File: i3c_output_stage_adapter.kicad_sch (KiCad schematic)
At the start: 52 parts, among them J1 PinSocket_2x12_P2.54mm_Drill1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, J2 PinSocket_2x6_P2.54mm_Drill1.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, J3 Molex_Nano-Fit_1x2_SMD_105430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, J4 PinHeader_2x5_P1.27mm_SMD, J5 PinHeader_2x5_P1.27mm_SMD, J6 JST_XH_1x3_S3B-XH-A-LF-SN, Q1 DMC2400UV-7, Q2 DMC2400UV-7, Q3 DMC2400UV-7, Q4 DMC2400UV-7, U1 TPS7A0518P_SOT23-5, U2 SN74LVC1G240_SC70, U3 SN74LVC1G240_SC70

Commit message: [#68164] Update schematic
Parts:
- removed D3: LED_G_0402_VLMTG1500-GS08, antmicro-footprints:LED_0402_1005Metric_G, symbol antmicroLEDIndicationDiscrete:LED_G_0402_VLMTG1500-GS08
- removed Q1, Q2: DMC2400UV-7, antmicro-footprints:SOT-563, symbol antmicroTransistorsFETsMOSFETsArrays:DMC2400UV-7
- removed R10, R19, R9: R_2k_0402, antmicro-footprints:R_0402_1005Metric, symbol antmicroResistors0402:R_2k_0402
- added MP1, MP2, MP3, MP4: MP_Pad6mm_Drill3.2mm, antmicro-footprints:MP_Pad6mm_Drill3.2mm, symbol antmicroMechanicalParts:MP_Pad6mm_Drill3.2mm
- added Q1, Q2: DMC31D5UDJ, antmicro-footprints:SOT-963, symbol antmicroTransistorsFETsMOSFETsArrays:DMC31D5UDJ
- added R10, R19, R20, R24: R_10k_0402, antmicro-footprints:R_0402_1005Metric, symbol antmicroResistors0402:R_10k_0402
- added R21, R25, R9: R_0R_0402, antmicro-footprints:R_0402_1005Metric, symbol antmicroResistors0402:R_0R_0402
- added R22, R23: R_2k_0402, antmicro-footprints:R_0402_1005Metric, symbol antmicroResistors0402:R_2k_0402
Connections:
- net +3V3: no longer R15.1
- net 1V8_LDO: no longer R17.2
- net GND: now also MP1.1, MP2.1, MP3.1, MP4.1, Q1.1 (S1), Q2.1 (S1), R10.1, R19.1, R23.1
- net SCL: now also J6.1, Q3.4 (S2), Q3.6 (D1), Q2.4 (S2), Q2.6 (D1); no longer J6.3
- net SCL_DOWN: now also R9.1; no longer Q3.2 (G1)
- net SCL_UP: now also R25.2; no longer Q3.5 (G2)
- net SDA: now also J6.3, Q1.4 (S2), Q1.6 (D1); no longer J6.1
- net SDA_DOWN: now also R15.1; no longer Q4.2 (G1)
- net SDA_UP: now also R21.2; no longer Q4.5 (G2)
- net at R6.1, R8.1: now also Q2.5 (G2)
- net at R2.2, R4.2: now also Q2.2 (G1)
- net at R1.2, R3.2: now also Q1.2 (G1)
- net at Q3.3 (D2): now also R22.1
- net at F1.1: now also Q1.3 (D2)
- net at R5.1, R7.1: now also Q1.5 (G2)
- net at F2.1: now also Q2.3 (D2)
- net at Q3.1 (S1): now also R23.2
- net VCC renamed +1V8
- net +1V8: now also R17.2, R20.2, R22.2, R24.2; no longer R15.2
- new net: Q4.5 (G2), R20.1, R21.1
- new net: Q3.2 (G1), R10.2, R9.2
- new net: Q3.5 (G2), R24.1, R25.1
- new net: Q4.2 (G1), R15.2, R19.2
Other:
- note added: "DISCRETE LOGIC"
- note added: "LINE DRIVER LOGIC"
- note removed: "VCC SELECT"
- moved on the sheet: C1, C2, D1, D2, J2, J3, J4, J5, J6, R12, R17, R18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

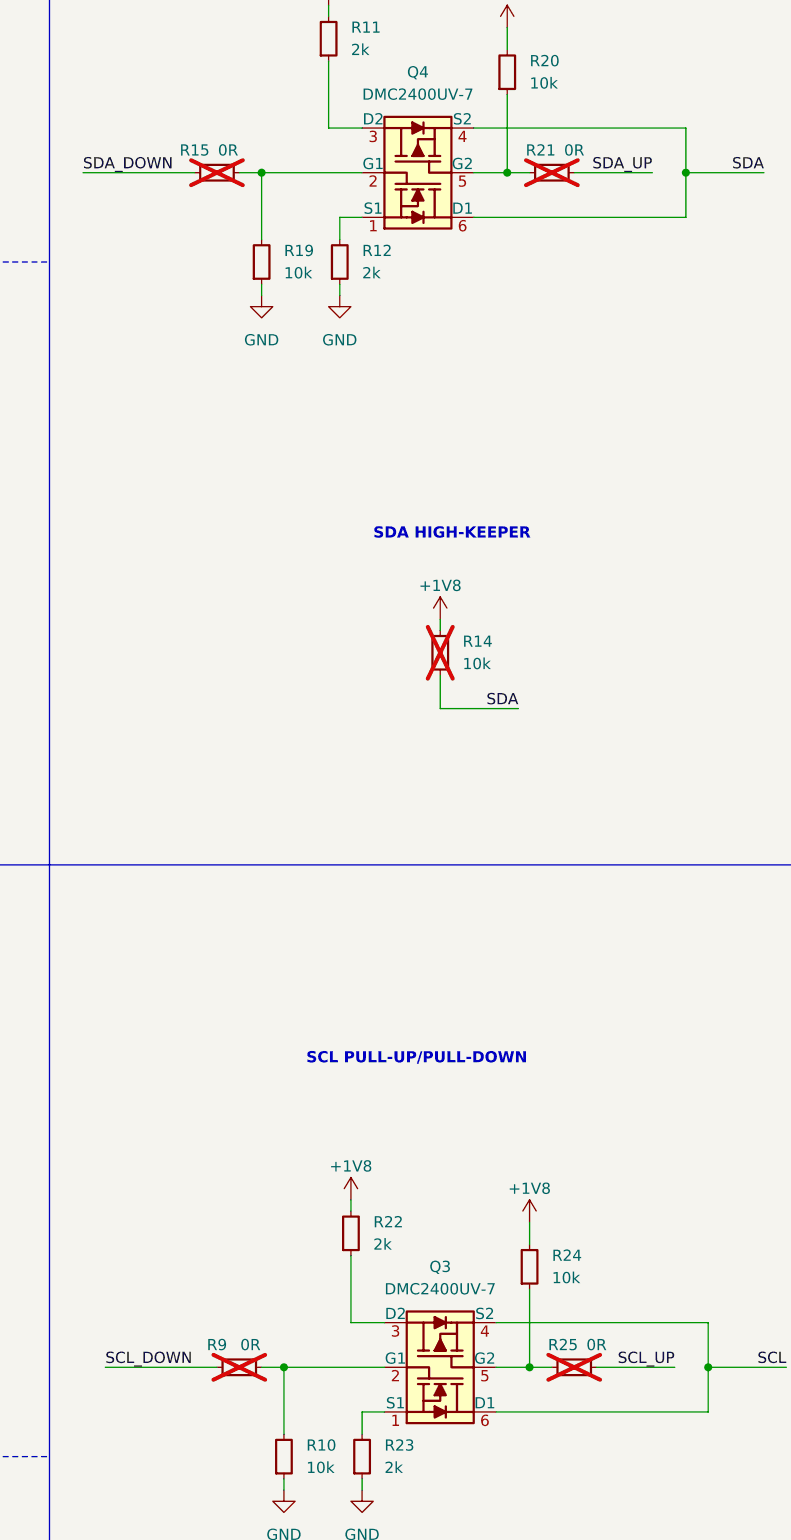
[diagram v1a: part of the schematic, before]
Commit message: [#68164] Populate resistors
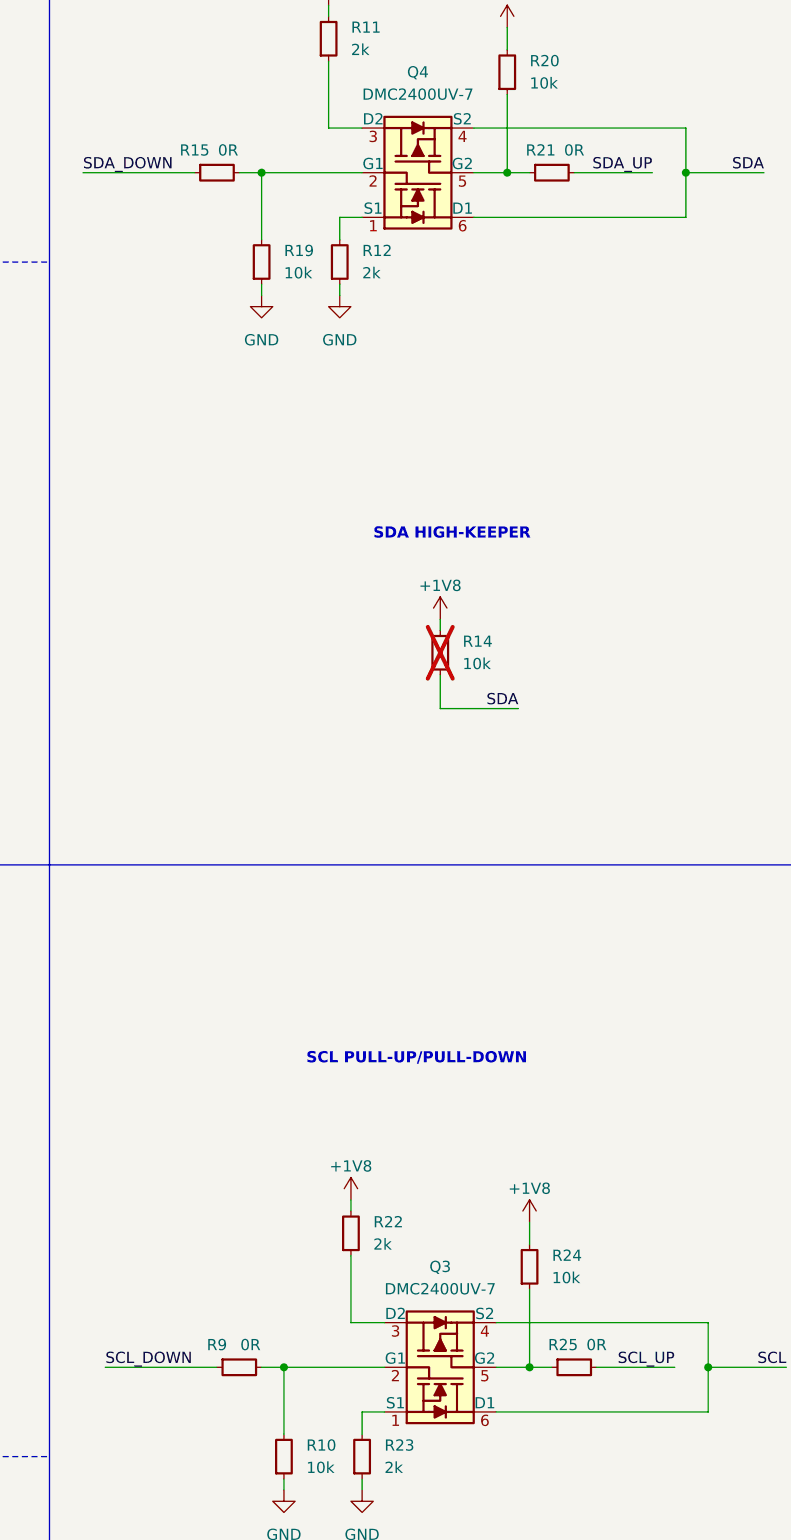
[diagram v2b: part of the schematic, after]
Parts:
- R15, R21, R25, R9: now fitted
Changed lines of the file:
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@@
   )
   (symbol (lib_id "antmicroResistors0402:R_0R_0402") (at 265.43 62.23 0) (unit 1)
-    (in_bom yes) (on_board yes) (dnp yes)
+    (in_bom yes) (on_board yes) (dnp no)
     (property "Reference" "R21" (at 266.7 59.69 0)
       (effects (font (size 1.27 1.27) (thickness 0.15)))
@@
   )
   (symbol (lib_id "antmicroResistors0402:R_0R_0402") (at 267.97 198.12 0) (unit 1)
-    (in_bom yes) (on_board yes) (dnp yes)
+    (in_bom yes) (on_board yes) (dnp no)
     (property "Reference" "R25" (at 269.24 195.58 0)
       (effects (font (size 1.27 1.27) (thickness 0.15)))
@@
   )
   (symbol (lib_id "antmicroResistors0402:R_0R_0402") (at 229.87 198.12 0) (unit 1)
-    (in_bom yes) (on_board yes) (dnp yes)
+    (in_bom yes) (on_board yes) (dnp no)
     (property "Reference" "R9" (at 229.87 195.58 0)
       (effects (font (size 1.27 1.27) (thickness 0.15)))
@@
   )
   (symbol (lib_id "antmicroResistors0402:R_0R_0402") (at 227.33 62.23 0) (unit 1)
-    (in_bom yes) (on_board yes) (dnp yes)
+    (in_bom yes) (on_board yes) (dnp no)
     (property "Reference" "R15" (at 227.33 59.69 0)
       (effects (font (size 1.27 1.27) (thickness 0.15)))

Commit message: [#68164] Clean ERC
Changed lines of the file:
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@@
   (junction (at 55.88 53.34) (diameter 0) (color 0 0 0 0)
   )
+  (junction (at 92.71 149.86) (diameter 0) (color 0 0 0 0)
+  )
+  (junction (at 50.8 157.48) (diameter 0) (color 0 0 0 0)
+  )
   (junction (at 368.3 236.22) (diameter 0) (color 0 0 0 0)
   )
@@
     (stroke (width 0) (type default))
   )
+  (wire (pts (xy 93.98 154.94) (xy 92.71 154.94))
+    (stroke (width 0) (type default))
+  )
   (wire (pts (xy 259.08 57.15) (xy 283.21 57.15))
     (stroke (width 0) (type default))
@@
     (stroke (width 0) (type default))
   )
+  (wire (pts (xy 92.71 149.86) (xy 93.98 149.86))
+    (stroke (width 0) (type default))
+  )
   (wire (pts (xy 261.62 198.12) (xy 265.43 198.12))
     (stroke (width 0) (type default))
@@
     (stroke (width 0) (type default))
   )
+  (wire (pts (xy 50.8 157.48) (xy 52.07 157.48))
+    (stroke (width 0) (type default))
+  )
   (wire (pts (xy 237.49 210.82) (xy 237.49 212.09))
     (stroke (width 0) (type default))
@@
     )
   )
+  (symbol (lib_id "antmicropower:PWR_FLAG") (at 93.98 149.86 270) (unit 1)
+    (in_bom yes) (on_board yes) (dnp no) (fields_autoplaced)
+    (property "Reference" "#FLG01" (at 95.885 149.86 0)
+      (effects (font (size 1.27 1.27)) hide)
+    )
+    (property "Value" "PWR_FLAG" (at 97.79 149.86 90)
+      (effects (font (size 1.27 1.27)) (justify left))
+    )
+    (property "Footprint" "" (at 93.98 149.86 0)
+      (effects (font (size 1.27 1.27)) hide)
+    )
+    (property "Datasheet" "" (at 93.98 149.86 0)
+      (effects (font (size 1.27 1.27)) hide)
+    )
+    (pin "1")
+    (instances
+      (project "i3c_output_stage_adapter"
+        (path "/612c5d43-2e76-4008-b7aa-7a9340e5e5ba"
+          (reference "#FLG01") (unit 1)
+        )
+      )
+    )
+  )
   (symbol (lib_id "antmicroResistors0402:R_0R_0402") (at 172.72 254 0) (unit 1)
     (in_bom yes) (on_board yes) (dnp yes)
@@
     )
   )
+  (symbol (lib_id "antmicropower:PWR_FLAG") (at 93.98 154.94 270) (unit 1)
+    (in_bom yes) (on_board yes) (dnp no) (fields_autoplaced)
+    (property "Reference" "#FLG02" (at 95.885 154.94 0)
+      (effects (font (size 1.27 1.27)) hide)
+    )
+    (property "Value" "PWR_FLAG" (at 97.79 154.94 90)
+      (effects (font (size 1.27 1.27)) (justify left))
+    )
+    (property "Footprint" "" (at 93.98 154.94 0)
+      (effects (font (size 1.27 1.27)) hide)
+    )
+    (property "Datasheet" "" (at 93.98 154.94 0)
+      (effects (font (size 1.27 1.27)) hide)
+    )
+    (pin "1")
+    (instances
+      (project "i3c_output_stage_adapter"
+        (path "/612c5d43-2e76-4008-b7aa-7a9340e5e5ba"
+          (reference "#FLG02") (unit 1)
+        )
+      )
+    )
+  )
   (symbol (lib_id "antmicropower:+1V8") (at 248.92 251.46 0) (unit 1)
     (in_bom yes) (on_board yes) (dnp no)
@@
         )
       )
+    )
+  )
+  (symbol (lib_id "antmicropower:PWR_FLAG") (at 52.07 157.48 270) (unit 1)
+    (in_bom yes) (on_board yes) (dnp no) (fields_autoplaced)
+    (property "Reference" "#FLG03" (at 53.975 157.48 0)
+      (effects (font (size 1.27 1.27)) hide)
+    )
+    (property "Value" "PWR_FLAG" (at 55.88 157.48 90)
+      (effects (font (size 1.27 1.27)) (justify left))
+    )
+    (property "Footprint" "" (at 52.07 157.48 0)
+      (effects (font (size 1.27 1.27)) hide)
+    )
+    (property "Datasheet" "" (at 52.07 157.48 0)
+      (effects (font (size 1.27 1.27)) hide)
+    )
+    (pin "1")
+    (instances
+      (project "i3c_output_stage_adapter"
+        (path "/612c5d43-2e76-4008-b7aa-7a9340e5e5ba"
+          (reference "#FLG03") (unit 1)
+        )
+      )

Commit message: [#68164] Clean DRC
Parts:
- removed J4, J5: PinHeader_2x5_P1.27mm_SMD, antmicro-footprints:PinHeader_2x5_P1.27mm_SMD, symbol antmicroGenericPinHeaders:PinHeader_2x5_P1.27mm_SMD
- added J7: PinHeader_2x10_P1.27mm_SMD, antmicro-footprints:PinHeader_2x10_P1.27mm_SMD, symbol antmicroGenericPinHeaders:PinHeader_2x10_P1.27mm_SMD
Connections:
- net GND: now also J7.1, J7.11, J7.13, J7.15, J7.17, J7.19, J7.3, J7.5, J7.7, J7.9
- net SCL: now also J7.12
- net SCL_DOWN: now also J7.20
- net SCL_EN/PULL: now also J7.16
- net SCL_IN/PUSH: now also J7.14
- net SCL_UP: now also J7.18
- net SDA: now also J7.2
- net SDA_DOWN: now also J7.10
- net SDA_EN/PULL: now also J7.6
- net SDA_IN/PUSH: now also J7.4
- net SDA_UP: now also J7.8
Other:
- moved on the sheet: J6, TP1, TP10, TP11, TP2, TP3, TP4, TP5, TP6, TP7, TP8, TP9

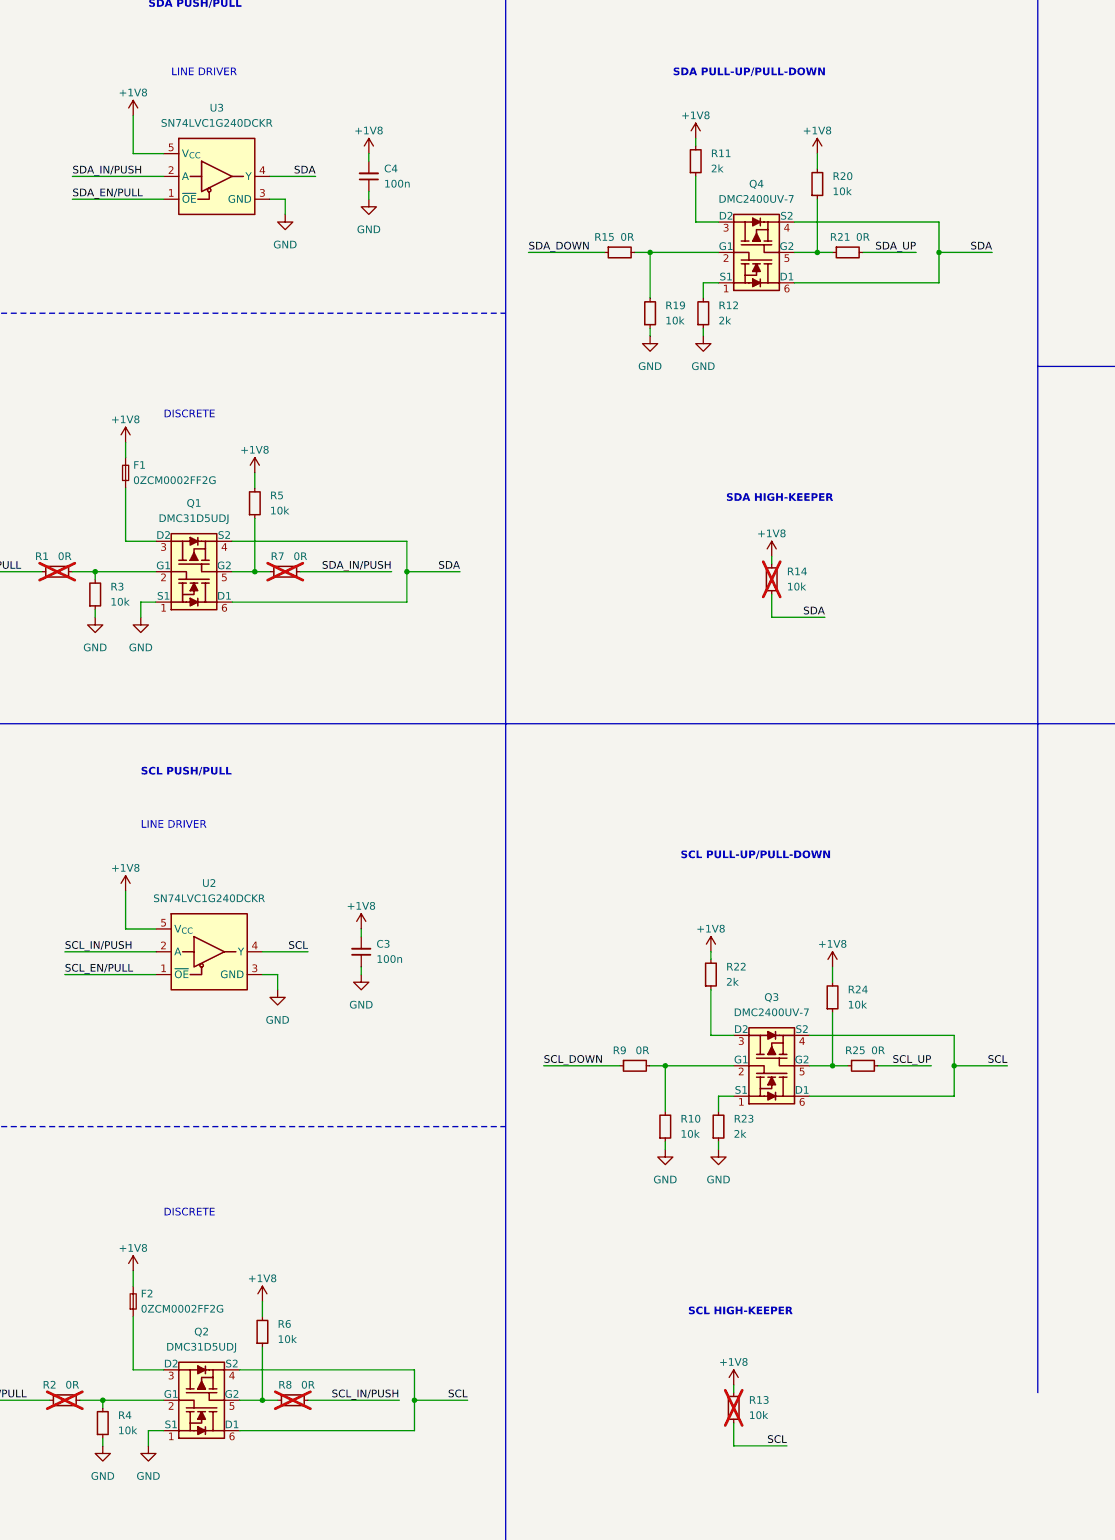
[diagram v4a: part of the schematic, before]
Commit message: [#68164] Update PMOS connections on schematic
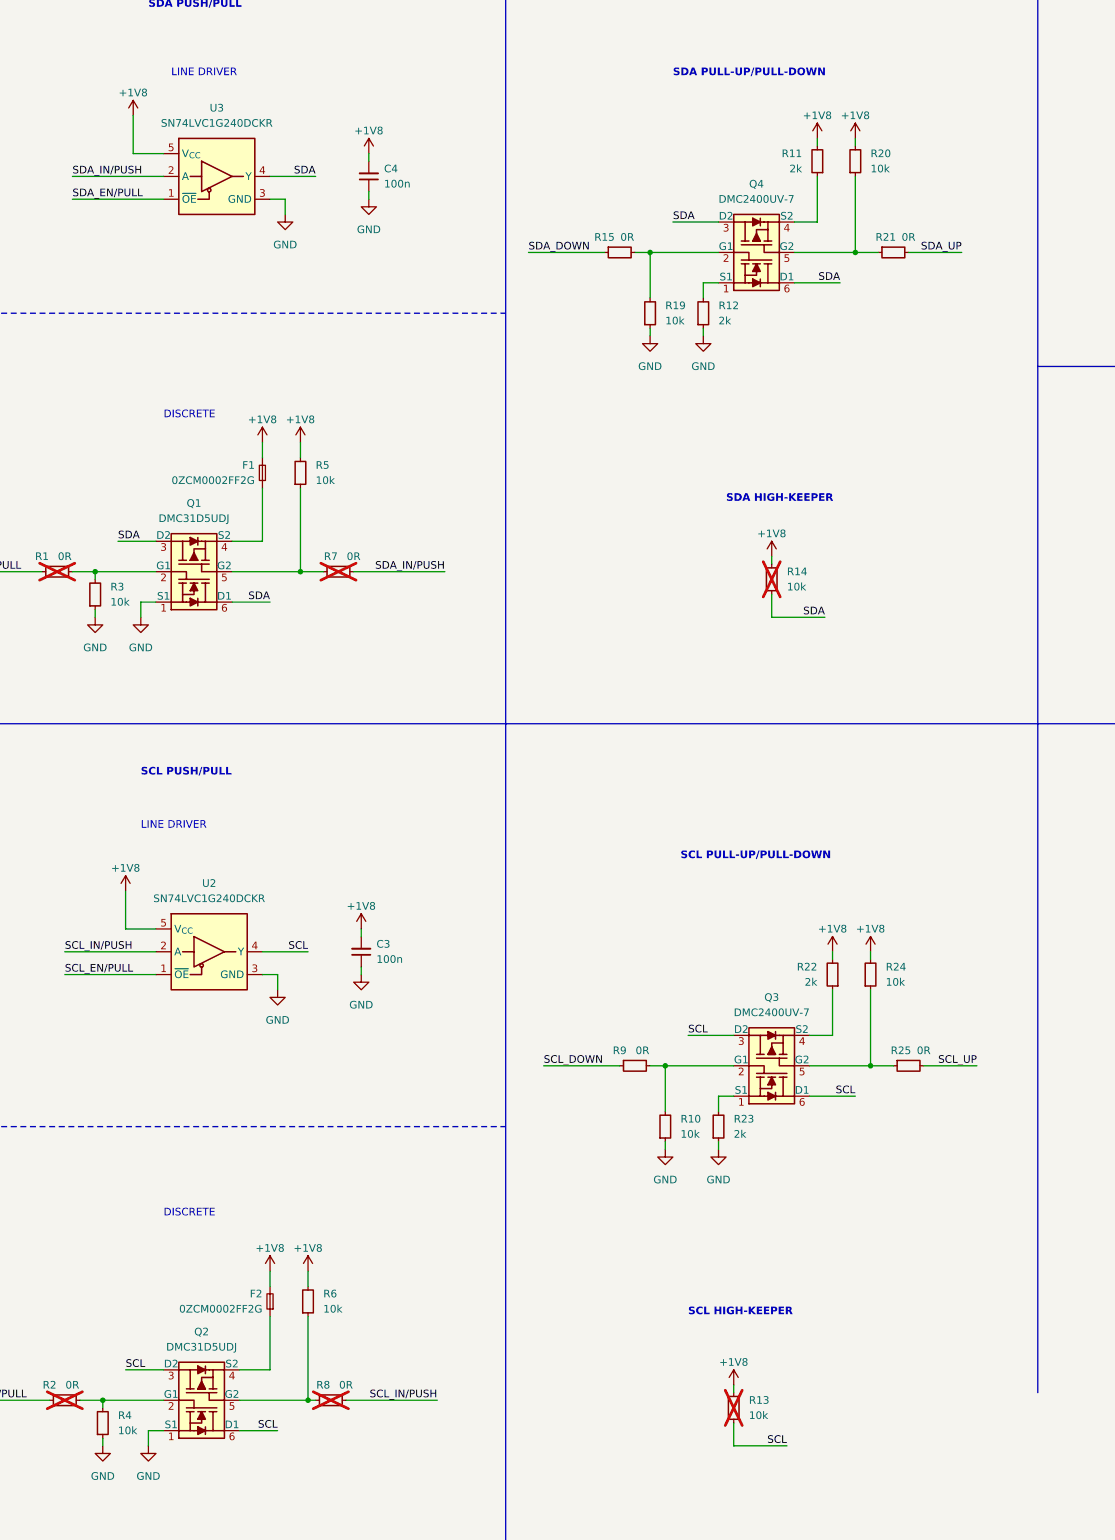
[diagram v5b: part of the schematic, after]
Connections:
- net SCL: now also Q2.3 (D2), Q3.3 (D2); no longer Q2.4 (S2), Q3.4 (S2)
- net SDA: now also Q1.3 (D2), Q4.3 (D2); no longer Q1.4 (S2), Q4.4 (S2)
- net at R22.1: now also Q3.4 (S2); no longer Q3.3 (D2)
- net at R11.1: now also Q4.4 (S2); no longer Q4.3 (D2)
- net at F2.1: now also Q2.4 (S2); no longer Q2.3 (D2)
- net at F1.1: now also Q1.4 (S2); no longer Q1.3 (D2)
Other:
- moved on the sheet: R20, R21, R24, R25, R5, R6, R7, R8

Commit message: [#68164] Add logos, align mounting holes
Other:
- moved on the sheet: D1, D2, R17, R18
